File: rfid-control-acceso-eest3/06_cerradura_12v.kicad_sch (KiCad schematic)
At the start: 5 parts, among them J9 LOCK_12V_1.8A_21.6W, Q2 AO3400A_PRELIM

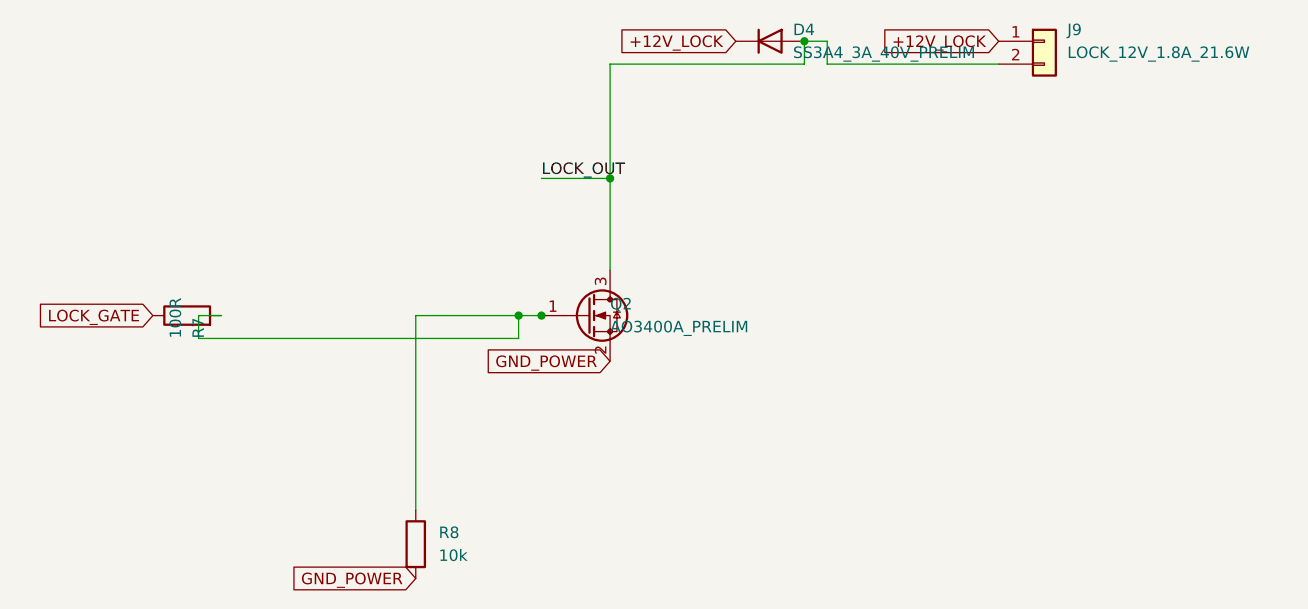
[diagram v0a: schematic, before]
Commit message: Reorganiza floorplan PCB Rev A antes del ruteo
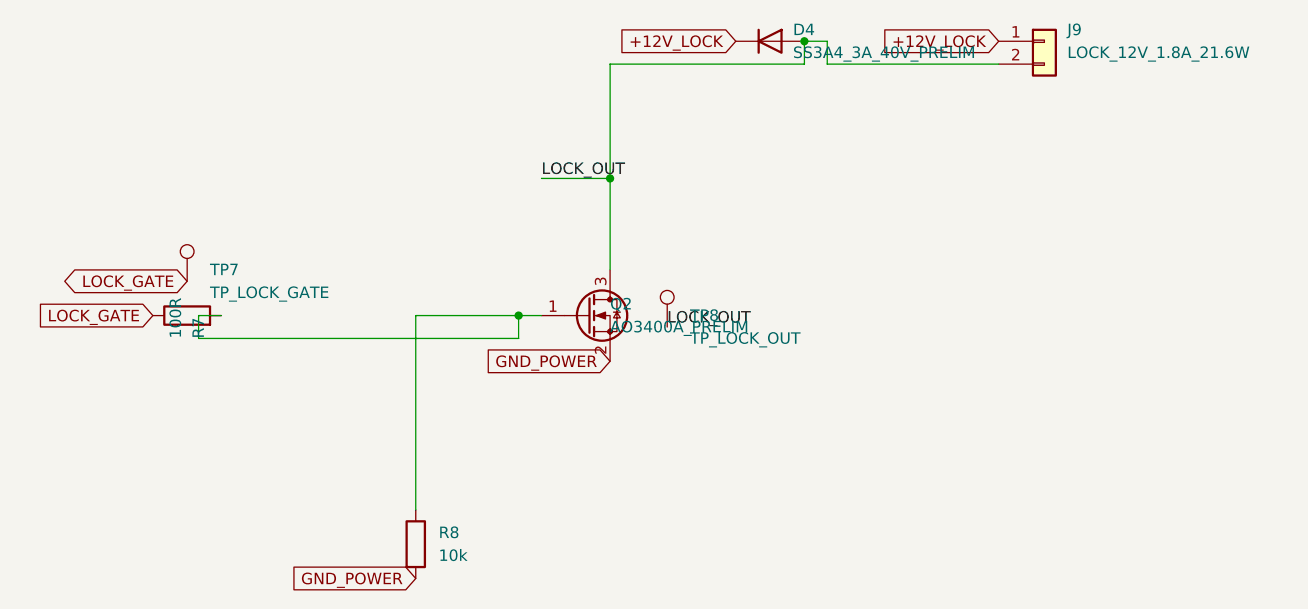
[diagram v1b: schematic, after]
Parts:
- added TP7: TP_LOCK_GATE, TestPoint:TestPoint_THTPad_D2.0mm_Drill1.0mm, symbol Connector:TestPoint
- added TP8: TP_LOCK_OUT, TestPoint:TestPoint_THTPad_D2.0mm_Drill1.0mm, symbol Connector:TestPoint
- D4: footprint (none) -> Diode_SMD:D_SMA
- J9: footprint (none) -> rfid_eest3:KF301_2P_P5.08_PLACEHOLDER_NO_FABRICAR
- Q2: footprint (none) -> Package_TO_SOT_SMD:SOT-23; Pinout_Verified (none) -> AO3400A AOS: 1=G, 2=S, 3=D
- R7, R8: footprint (none) -> Resistor_THT:R_Axial_DIN0207_L6.3mm_D2.5mm_P10.16mm_Horizontal
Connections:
- net LOCK_GATE: now also TP7.1
- net LOCK_OUT: now also TP8.1
